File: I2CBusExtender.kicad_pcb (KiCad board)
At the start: 2 copper layers, 19 parts, among them J1 SBusConn, J2 LBusCon, U1 P82B715

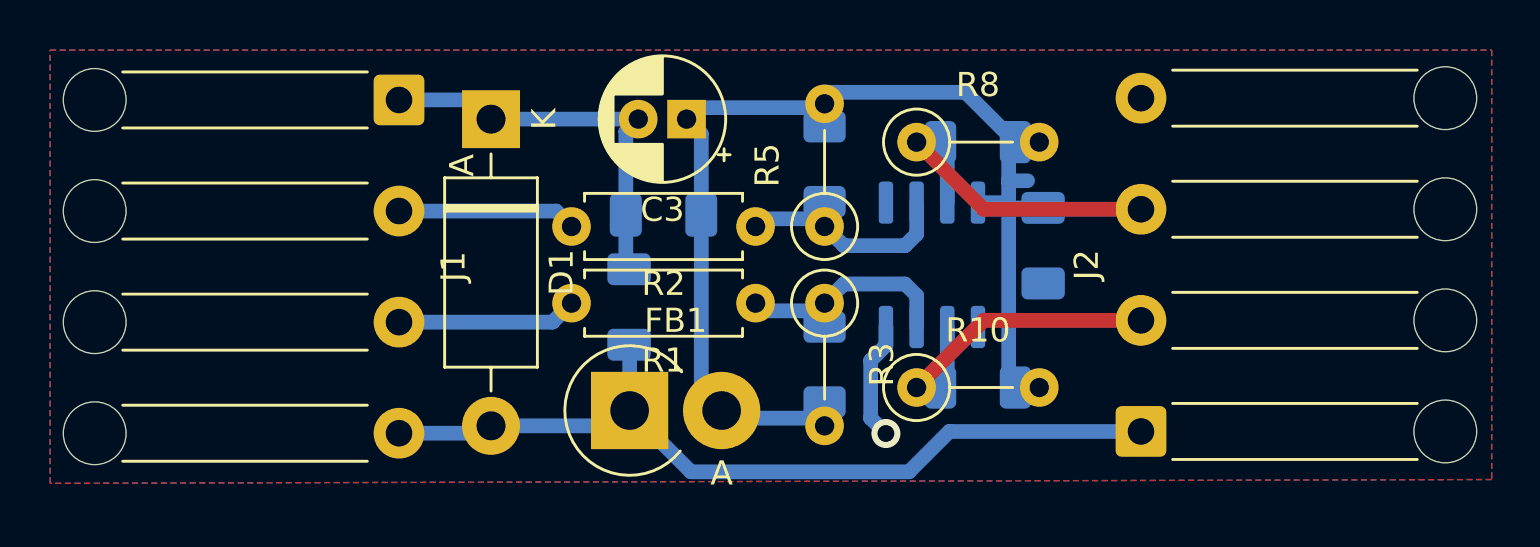
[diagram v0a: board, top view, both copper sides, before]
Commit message: Tweaked schematic layout and improved board design to the point it passes DRC.
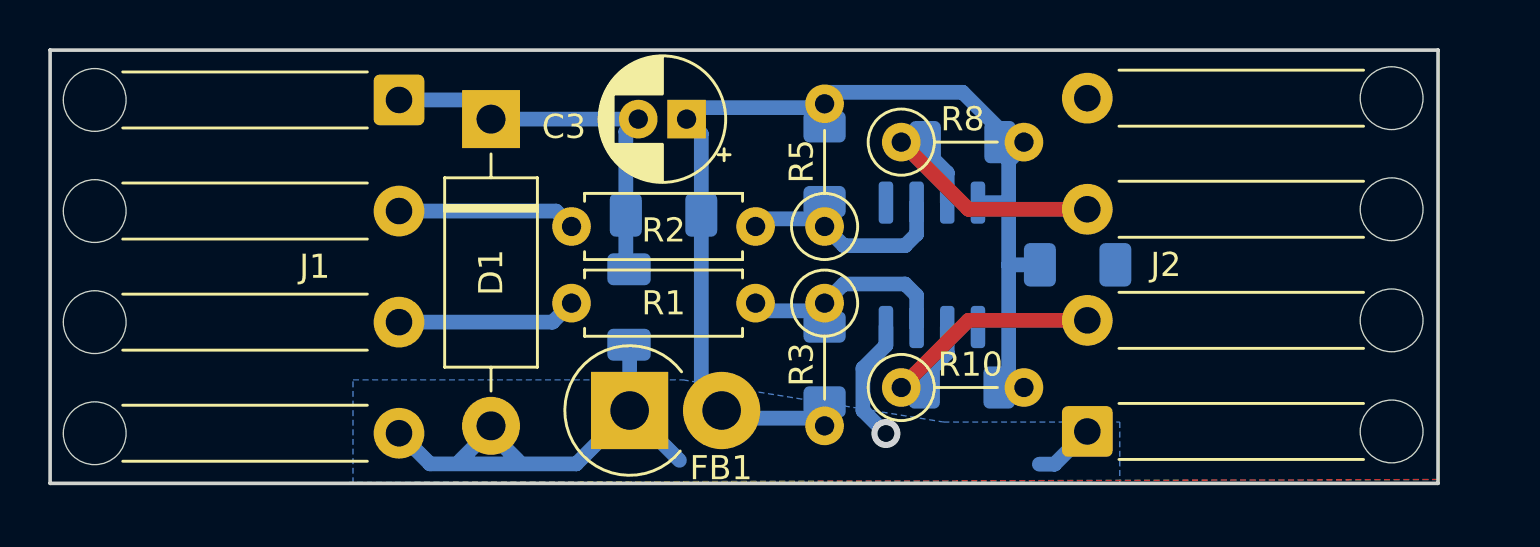
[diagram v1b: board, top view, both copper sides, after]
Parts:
- moved J2 2.22 mm to (116.4, 93.1)
- moved C4 1.63 mm to (116.0, 86.2), turned to 0 degrees
- moved R9 0.67 mm to (111.2, 91.3)
- moved R7 0.64 mm to (111.3, 81.1)
- moved R10 0.63 mm to (108.7, 91.3)
- moved R8 0.63 mm to (108.7, 81.1)
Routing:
- net /Pwr: track 35.6 -> 21.7 mm
- net Net-(J2-Pad3): track 13.2 -> 11.4 mm
- net /VCC: track 49.0 -> 47.6 mm
- added copper zone on B.Cu, net /Pwr
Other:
- board outline added: 57.5 x 17.9 mm

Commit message: Tweaked layouts and footprints.
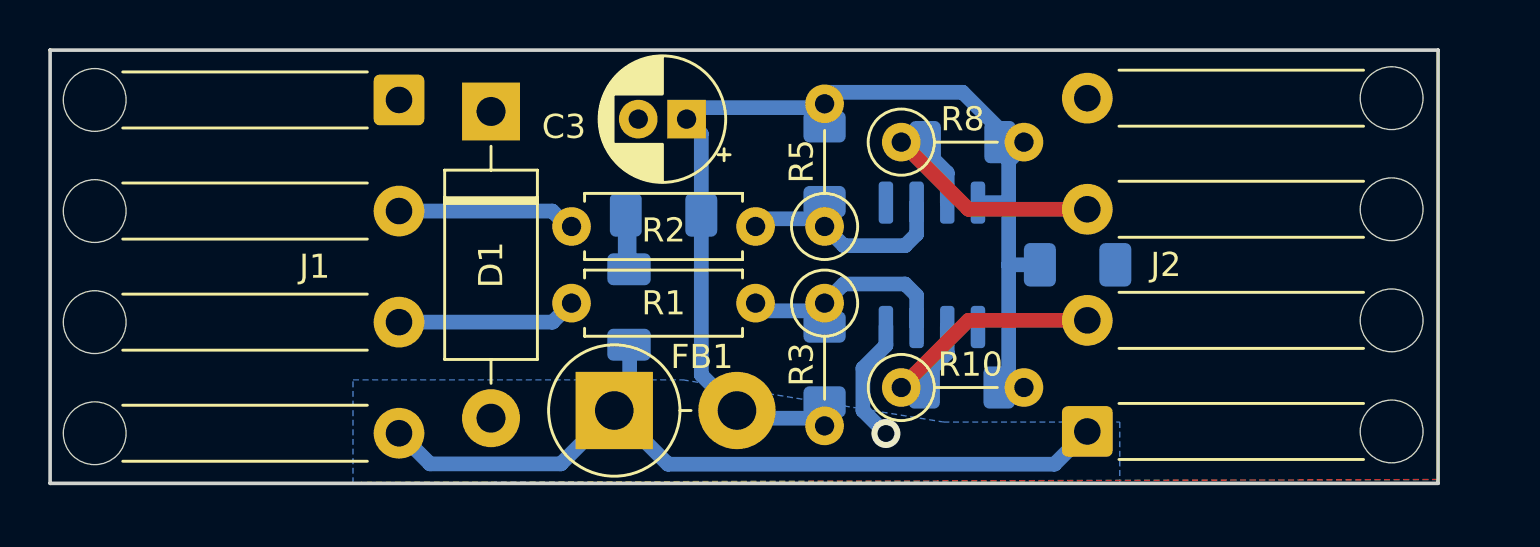
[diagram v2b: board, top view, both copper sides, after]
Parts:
- FB1: footprint Diode_THT:D_DO-201AD_P3.81mm_Vertical_AnodeUp -> Diode_THT:D_DO-201AD_P5.08mm_Vertical_AnodeUp
- moved FB1 0.64 mm to (96.9, 92.2)
- moved D1 0.32 mm to (91.8, 79.9)
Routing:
- net /Pwr: track 21.7 -> 34.2 mm
- net /Gnd: track 21.9 -> 9.49 mm
- net /VCC: track 47.6 -> 47.0 mm

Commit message: Tidied up track layout to make track rounding and filleting work better.
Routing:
- net /Pwr: track 34.2 -> 36.0 mm
- net /VCC: track 47.0 -> 45.5 mm
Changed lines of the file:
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@@
   )
   (footprint "Resistor_SMD:R_1206_3216Metric_Pad1.30x1.75mm_HandSolder" (layer "B.Cu")
-    (at 111.24625 91.28125)
+    (at 111.28375 91.28125)
     (descr "Resistor SMD 1206 (3216 Metric), square (rectangular) end terminal, IPC_7351 nominal with elongated pad for handsoldering. (Body size source: IPC-SM-782 page 72, https://www.pcb-3d.com/wordpress/wp-content/uploads/ipc-sm-782a_amendment_1_and_2.pdf), generated with kicad-footprint-generator")
     (tags "resistor handsolder")
@@
   )
   (footprint "Resistor_SMD:R_1206_3216Metric_Pad1.30x1.75mm_HandSolder" (layer "B.Cu")
-    (at 105.56875 82.03625 90)
+    (at 105.56875 82.07375 90)
     (descr "Resistor SMD 1206 (3216 Metric), square (rectangular) end terminal, IPC_7351 nominal with elongated pad for handsoldering. (Body size source: IPC-SM-782 page 72, https://www.pcb-3d.com/wordpress/wp-content/uploads/ipc-sm-782a_amendment_1_and_2.pdf), generated with kicad-footprint-generator")
     (tags "resistor handsolder")
@@
   (segment (start 105.25125 84.29625) (end 105.56875 84.61375) (width 0.6096) (layer "B.Cu") (net 2))
   (segment (start 99.08375 94.45625) (end 96.86125 92.23375) (width 0.6096) (layer "B.Cu") (net 3))
-  (segment (start 87.96 93.175) (end 89.229375 94.444375) (width 0.6096) (layer "B.Cu") (net 3))
   (segment (start 116.4475 93.10125) (end 115.0925 94.45625) (width 0.6096) (layer "B.Cu") (net 3))
-  (segment (start 94.650625 94.444375) (end 96.86125 92.23375) (width 0.6096) (layer "B.Cu") (net 3))
   (segment (start 97.49625 89.53375) (end 97.4725 89.51) (width 0.6096) (layer "B.Cu") (net 3))
   (segment (start 87.9475 93.175) (end 87.96 93.175) (width 0.6096) (layer "B.Cu") (net 3))
   (segment (start 115.0925 94.45625) (end 99.08375 94.45625) (width 0.6096) (layer "B.Cu") (net 3))
   (segment (start 97.49625 92.23375) (end 97.49625 89.53375) (width 0.6096) (layer "B.Cu") (net 3))
-  (segment (start 89.229375 94.444375) (end 94.650625 94.444375) (width 0.6096) (layer "B.Cu") (net 3))
-  (via (at 108.10875 93.18625) (size 1.2) (drill 0.7) (layers "F.Cu" "B.Cu") (net 4))
+  (segment (start 94.6625 94.4325) (end 96.86125 92.23375) (width 0.6096) (layer "B.Cu") (net 3))
+  (segment (start 91.7575 94.4325) (end 89.205 94.4325) (width 0.6096) (layer "B.Cu") (net 3))
+  (segment (start 89.205 94.4325) (end 87.9475 93.175) (width 0.6096) (layer "B.Cu") (net 3))
+  (segment (start 91.7575 94.4325) (end 94.6625 94.4325) (width 0.6096) (layer "B.Cu") (net 3))
+  (segment (start 91.7575 92.55125) (end 91.7575 94.4325) (width 0.6096) (layer "B.Cu") (net 3))
+  (via (at 108.10875 93.18625) (size 1.3) (drill 0.7) (layers "F.Cu" "B.Cu") (net 4))
   (segment (start 97.4725 86.385) (end 97.4725 84.29625) (width 0.6096) (layer "B.Cu") (net 4))
   (segment (start 108.10875 88.77625) (end 108.10875 89.535) (width 0.6096) (layer "B.Cu") (net 4))
+  (segment (start 108.10875 89.535) (end 107.15625 90.4875) (width 0.6096) (layer "B.Cu") (net 4))
+  (segment (start 107.15625 92.23375) (end 108.10875 93.18625) (width 0.6096) (layer "B.Cu") (net 4))
   (segment (start 107.15625 90.4875) (end 107.15625 92.23375) (width 0.6096) (layer "B.Cu") (net 4))
   (segment (start 97.31375 84.1625) (end 97.31375 86.36) (width 0.6096) (layer "B.Cu") (net 4))
-  (segment (start 108.10875 89.535) (end 107.15625 90.4875) (width 0.6096) (layer "B.Cu") (net 4))
-  (segment (start 107.15625 92.23375) (end 108.10875 93.18625) (width 0.6096) (layer "B.Cu") (net 4))
   (segment (start 87.9475 83.975) (end 94.29375 83.975) (width 0.6096) (layer "B.Cu") (net 5))
   (segment (start 94.29375 83.975) (end 95.25 84.93125) (width 0.6096) (layer "B.Cu") (net 5))
@@
   (segment (start 110.64875 82.39125) (end 109.69625 81.43875) (width 0.6096) (layer "B.Cu") (net 8))
   (segment (start 110.64875 83.62625) (end 110.64875 82.39125) (width 0.6096) (layer "B.Cu") (net 8))
-  (segment (start 105.56875 92.86875) (end 105.56875 91.87875) (width 0.6096) (layer "B.Cu") (net 9))
-  (segment (start 105.56875 92.86875) (end 105.25125 92.55125) (width 0.6096) (layer "B.Cu") (net 9))
   (segment (start 102.25875 92.55125) (end 101.94125 92.23375) (width 0.6096) (layer "B.Cu") (net 9))
   (segment (start 114.48375 86.20125) (end 113.18875 86.20125) (width 0.6096) (layer "B.Cu") (net 9))
-  (segment (start 113.665 81.12125) (end 113.6275 81.12125) (width 0.6096) (layer "B.Cu") (net 9))
+  (segment (start 111.125 79.0575) (end 107.315 79.0575) (width 0.6096) (layer "B.Cu") (net 9))
+  (segment (start 113.18875 86.20125) (end 113.18875 83.62625) (width 0.6096) (layer "B.Cu") (net 9))
+  (segment (start 106.9975 79.375) (end 105.7275 80.645) (width 0.6096) (layer "B.Cu") (net 9))
+  (segment (start 106.9975 79.375) (end 107.315 79.0575) (width 0.6096) (layer "B.Cu") (net 9))
+  (segment (start 112.55375 80.48625) (end 111.125 79.0575) (width 0.6096) (layer "B.Cu") (net 9))
   (segment (start 100.46375 84.1375) (end 100.46375 90.75625) (width 0.6096) (layer "B.Cu") (net 9))
-  (segment (start 113.18875 81.12125) (end 113.46875 81.12125) (width 0.6096) (layer "B.Cu") (net 9))
-  (segment (start 105.56875 79.0575) (end 111.28375 79.0575) (width 0.6096) (layer "B.Cu") (net 9))
   (segment (start 100.46375 84.1375) (end 100.46375 80.77875) (width 0.6096) (layer "B.Cu") (net 9))
+  (segment (start 104.4575 79.6925) (end 105.25125 80.48625) (width 0.6096) (layer "B.Cu") (net 9))
+  (segment (start 105.7275 79.375) (end 106.9975 79.375) (width 0.6096) (layer "B.Cu") (net 9))
+  (segment (start 104.4575 79.6925) (end 100.33 79.6925) (width 0.6096) (layer "B.Cu") (net 9))
+  (segment (start 113.18875 83.62625) (end 113.18875 81.75625) (width 0.6096) (layer "B.Cu") (net 9))
+  (segment (start 99.85375 80.16875) (end 100.46375 80.77875) (width 0.6096) (layer "B.Cu") (net 9))
+  (segment (start 104.4575 79.6925) (end 105.56875 79.6925) (width 0.6096) (layer "B.Cu") (net 9))
+  (segment (start 105.25125 92.55125) (end 102.25875 92.55125) (width 0.6096) (layer "B.Cu") (net 9))
+  (segment (start 113.18875 81.75625) (end 113.82375 81.12125) (width 0.6096) (layer "B.Cu") (net 9))
+  (segment (start 100.46375 90.75625) (end 101.94125 92.23375) (width 0.6096) (layer "B.Cu") (net 9))
+  (segment (start 113.18875 83.62625) (end 111.91875 83.62625) (width 0.6096) (layer "B.Cu") (net 9))
+  (segment (start 113.18875 91.00125) (end 113.18875 86.20125) (width 0.6096) (layer "B.Cu") (net 9))
   (segment (start 100.33 79.6925) (end 99.85375 80.16875) (width 0.6096) (layer "B.Cu") (net 9))
-  (segment (start 105.56875 79.6925) (end 100.33 79.6925) (width 0.6096) (layer "B.Cu") (net 9))
-  (segment (start 105.56875 79.53375) (end 105.56875 79.0575) (width 0.6096) (layer "B.Cu") (net 9))
-  (segment (start 105.88625 79.375) (end 105.56875 79.6925) (width 0.6096) (layer "B.Cu") (net 9))
-  (segment (start 111.28375 79.0575) (end 113.03 80.80375) (width 0.6096) (layer "B.Cu") (net 9))
-  (segment (start 105.56875 79.53375) (end 105.56875 80.48625) (width 0.6096) (layer "B.Cu") (net 9))
-  (segment (start 100.46375 80.77875) (end 99.85375 80.16875) (width 0.6096) (layer "B.Cu") (net 9))
-  (segment (start 113.18875 86.20125) (end 113.18875 83.82) (width 0.6096) (layer "B.Cu") (net 9))
-  (segment (start 105.25125 92.55125) (end 102.25875 92.55125) (width 0.6096) (layer "B.Cu") (net 9))
-  (segment (start 113.18875 81.40125) (end 113.46875 81.12125) (width 0.6096) (layer "B.Cu") (net 9))
-  (segment (start 100.46375 90.75625) (end 101.94125 92.23375) (width 0.6096) (layer "B.Cu") (net 9))
-  (segment (start 113.18875 83.62625) (end 113.18875 81.915) (width 0.6096) (layer "B.Cu") (net 9))
-  (segment (start 113.18875 83.82) (end 113.18875 83.62625) (width 0.6096) (layer "B.Cu") (net 9))
-  (segment (start 113.18875 83.62625) (end 111.91875 83.62625) (width 0.6096) (layer "B.Cu") (net 9))
-  (segment (start 113.18875 81.915) (end 113.82375 81.28) (width 0.6096) (layer "B.Cu") (net 9))
-  (segment (start 113.18875 91.00125) (end 113.18875 86.20125) (width 0.6096) (layer "B.Cu") (net 9))
   (zone (net 4) (net_name "/Gnd") (layers F&B.Cu) (name "GroundPlanes") (hatch edge 0.508)
     (connect_pads (clearance 0.508))

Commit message: Added silk screen pad labels and tidied up a track.
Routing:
- net /Pwr: track 36.0 -> 40.4 mm
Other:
- board text added: "Gnd"
- board text added: "LCL"
- board text added: "LDA"
- board text added: "SCL"
- board text added: "SDA"
- board text added: "Vcc"
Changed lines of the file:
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@@
     (property "Sheetname" "")
     (attr exclude_from_pos_files)
-    (fp_text reference "J2" (at 6.9 3.25 180) (layer "F.SilkS")
+    (fp_text reference "J2" (at 6.9 3.25 180) (layer "F.SilkS") hide
       (effects (font (size 1 1) (thickness 0.15)))
     )
@@
     (property "Sheetname" "")
     (attr exclude_from_pos_files)
-    (fp_text reference "J1" (at 6.9 3.4925 180) (layer "F.SilkS")
+    (fp_text reference "J1" (at 6.9 3.4925 180) (layer "F.SilkS") hide
       (effects (font (size 1 1) (thickness 0.15)))
     )
@@
   )
   (gr_rect (start 73.50125 77.31125) (end 130.96875 95.25) (layer "Edge.Cuts") (width 0.15) (fill none))
+  (gr_text "SCL" (at 81.43875 88.5825) (layer "F.SilkS")
+    (effects (font (size 1 1) (thickness 0.15)))
+  )
+  (gr_text "Gnd" (at 122.8725 79.375) (layer "F.SilkS")
+    (effects (font (size 1 1) (thickness 0.15)))
+  )
+  (gr_text "SDA" (at 81.43875 83.97875) (layer "F.SilkS")
+    (effects (font (size 1 1) (thickness 0.15)))
+  )
+  (gr_text "Gnd" (at 81.43875 79.375) (layer "F.SilkS")
+    (effects (font (size 1 1) (thickness 0.15)))
+  )
+  (gr_text "Vcc" (at 81.43875 93.18625) (layer "F.SilkS")
+    (effects (font (size 1 1) (thickness 0.15)))
+  )
+  (gr_text "Vcc" (at 122.8725 93.18625) (layer "F.SilkS")
+    (effects (font (size 1 1) (thickness 0.15)))
+  )
+  (gr_text "LCL" (at 122.8725 88.5825) (layer "F.SilkS")
+    (effects (font (size 1 1) (thickness 0.15)))
+  )
+  (gr_text "LDA" (at 122.8725 83.97875) (layer "F.SilkS")
+    (effects (font (size 1 1) (thickness 0.15)))
+  )
   (segment (start 109.37875 87.47125) (end 108.9025 86.995) (width 0.6096) (layer "B.Cu") (net 1))
   (segment (start 108.9025 86.995) (end 106.3625 86.995) (width 0.6096) (layer "B.Cu") (net 1))
@@
   (segment (start 106.3625 85.4075) (end 105.56875 84.61375) (width 0.6096) (layer "B.Cu") (net 2))
   (segment (start 105.25125 84.29625) (end 105.56875 84.61375) (width 0.6096) (layer "B.Cu") (net 2))
-  (segment (start 99.08375 94.45625) (end 96.86125 92.23375) (width 0.6096) (layer "B.Cu") (net 3))
-  (segment (start 116.4475 93.10125) (end 115.0925 94.45625) (width 0.6096) (layer "B.Cu") (net 3))
+  (segment (start 115.11625 94.4325) (end 101.94125 94.4325) (width 0.6096) (layer "B.Cu") (net 3))
+  (segment (start 116.4475 93.10125) (end 115.11625 94.4325) (width 0.6096) (layer "B.Cu") (net 3))
   (segment (start 97.49625 89.53375) (end 97.4725 89.51) (width 0.6096) (layer "B.Cu") (net 3))
   (segment (start 87.9475 93.175) (end 87.96 93.175) (width 0.6096) (layer "B.Cu") (net 3))
-  (segment (start 115.0925 94.45625) (end 99.08375 94.45625) (width 0.6096) (layer "B.Cu") (net 3))
   (segment (start 97.49625 92.23375) (end 97.49625 89.53375) (width 0.6096) (layer "B.Cu") (net 3))
   (segment (start 94.6625 94.4325) (end 96.86125 92.23375) (width 0.6096) (layer "B.Cu") (net 3))
+  (segment (start 94.6625 94.4325) (end 99.06 94.4325) (width 0.6096) (layer "B.Cu") (net 3))
   (segment (start 91.7575 94.4325) (end 89.205 94.4325) (width 0.6096) (layer "B.Cu") (net 3))
+  (segment (start 99.06 94.4325) (end 101.94125 94.4325) (width 0.6096) (layer "B.Cu") (net 3))
+  (segment (start 99.06 94.4325) (end 96.86125 92.23375) (width 0.6096) (layer "B.Cu") (net 3))
   (segment (start 89.205 94.4325) (end 87.9475 93.175) (width 0.6096) (layer "B.Cu") (net 3))
   (segment (start 91.7575 94.4325) (end 94.6625 94.4325) (width 0.6096) (layer "B.Cu") (net 3))

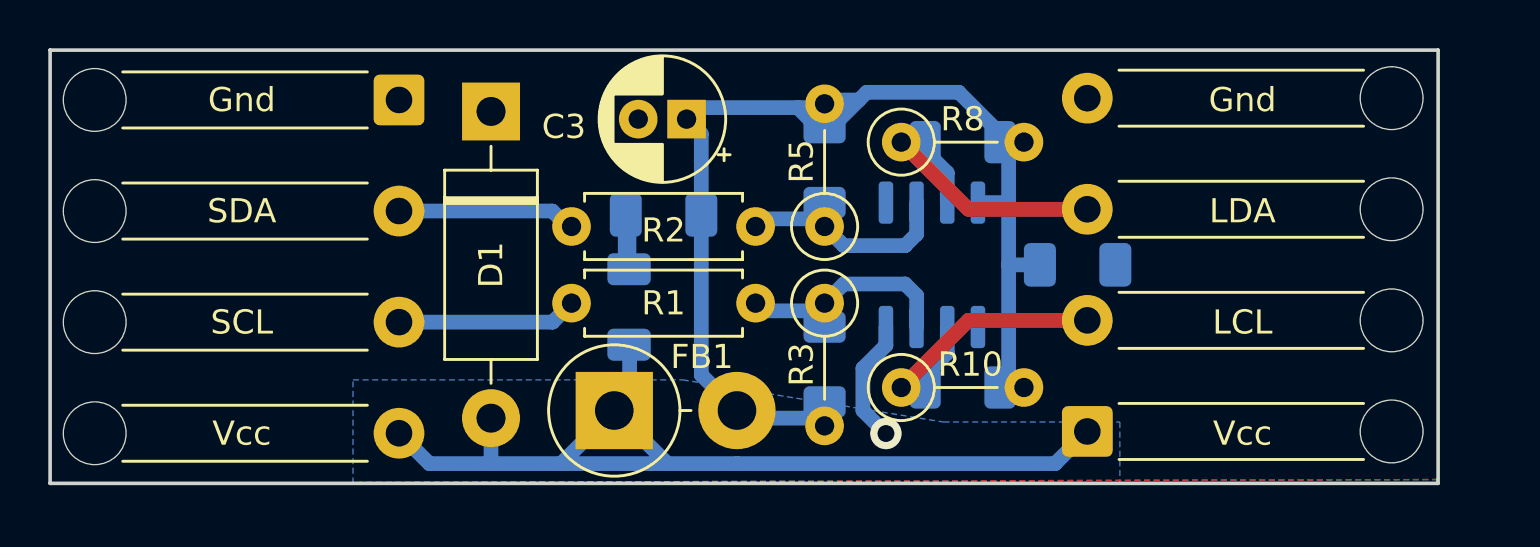
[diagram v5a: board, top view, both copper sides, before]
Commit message: Added new ferrite bead footprint to PCB.
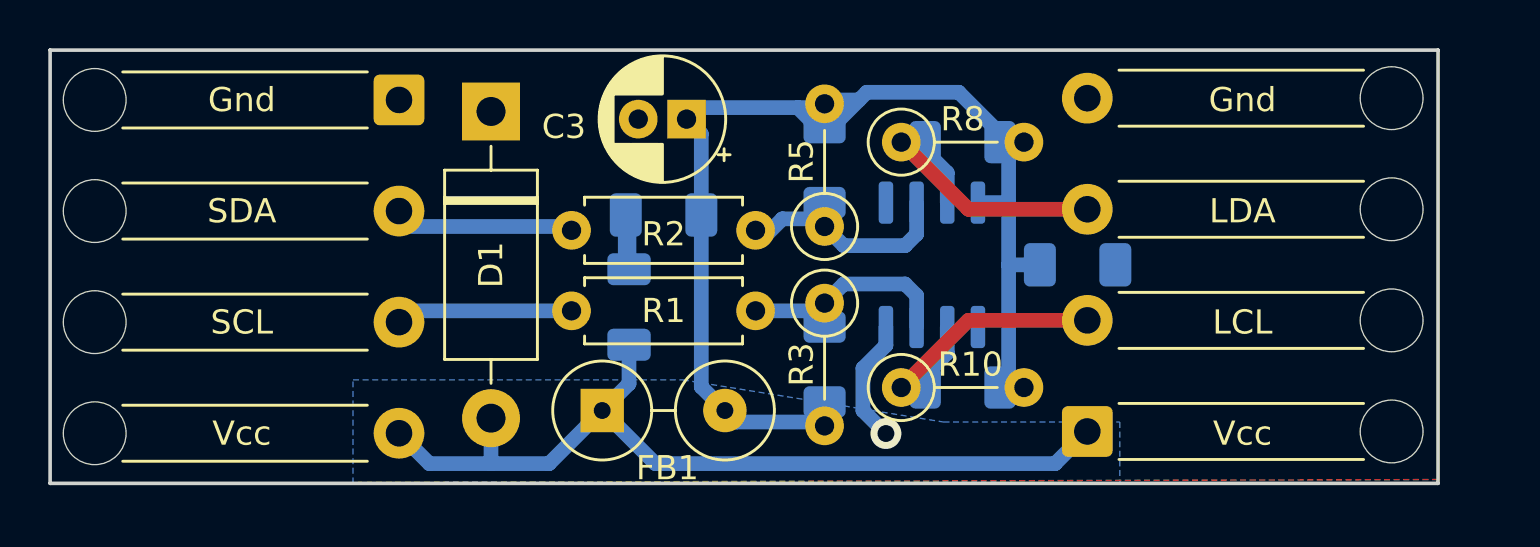
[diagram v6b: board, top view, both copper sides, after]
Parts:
- FB1: footprint Diode_THT:D_DO-201AD_P5.08mm_Vertical_AnodeUp -> I2CBusExtender:EXCEL_DR35C
- moved FB1 0.50 mm to (96.4, 92.2)
- moved R1 0.32 mm to (102.7, 88.1)
- moved R2 0.16 mm to (102.7, 84.8)
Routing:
- net /Pwr: track 40.4 -> 36.5 mm
- net Net-(J1-Pad2): track 7.70 -> 7.14 mm
